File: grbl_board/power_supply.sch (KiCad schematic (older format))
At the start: 24 parts

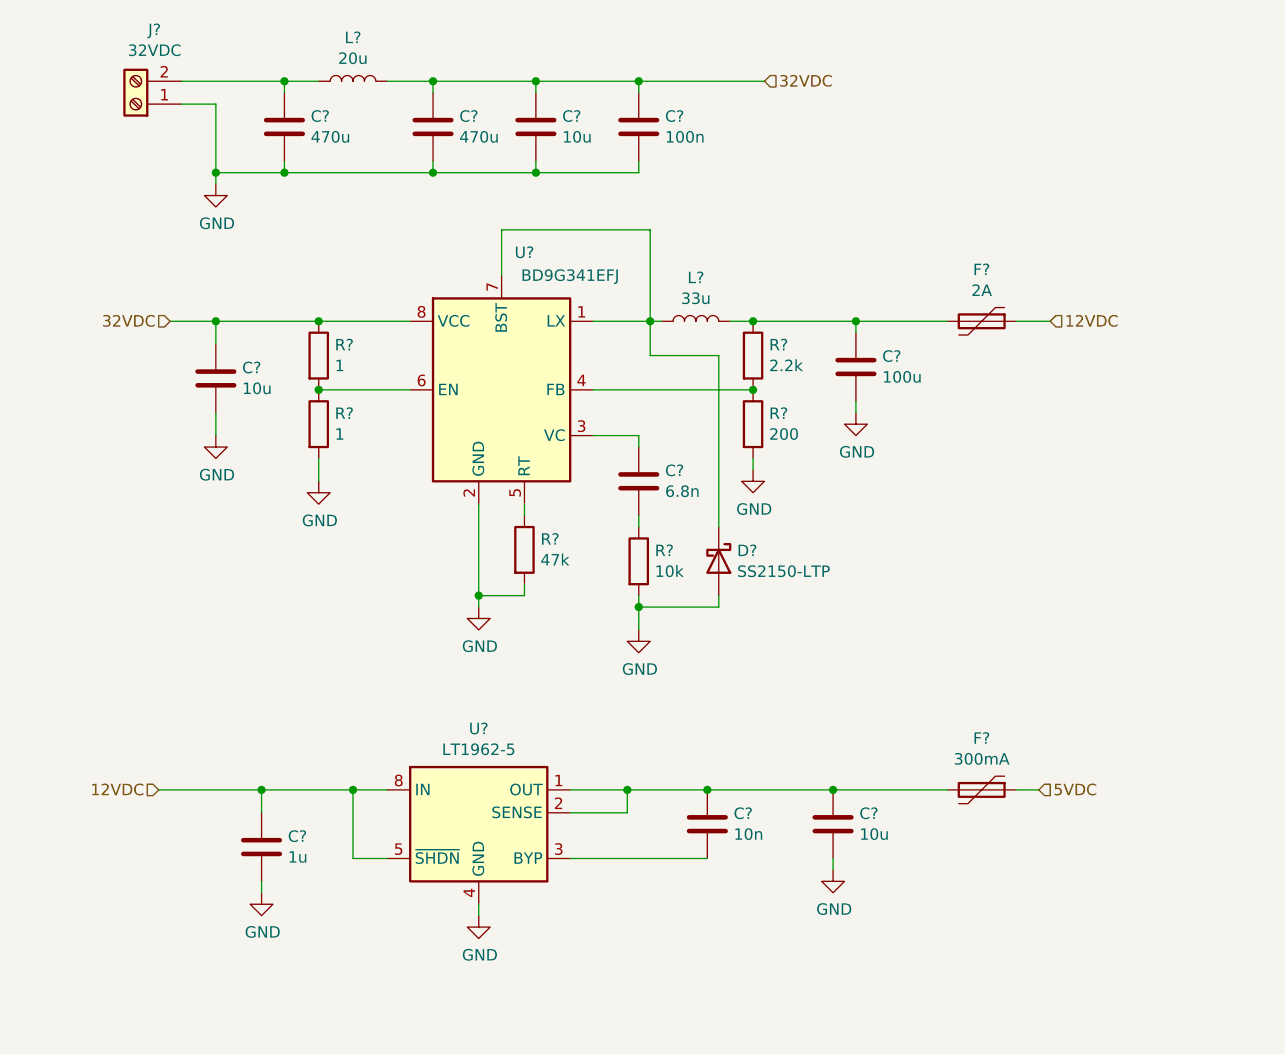
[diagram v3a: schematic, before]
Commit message: added some footprint associations
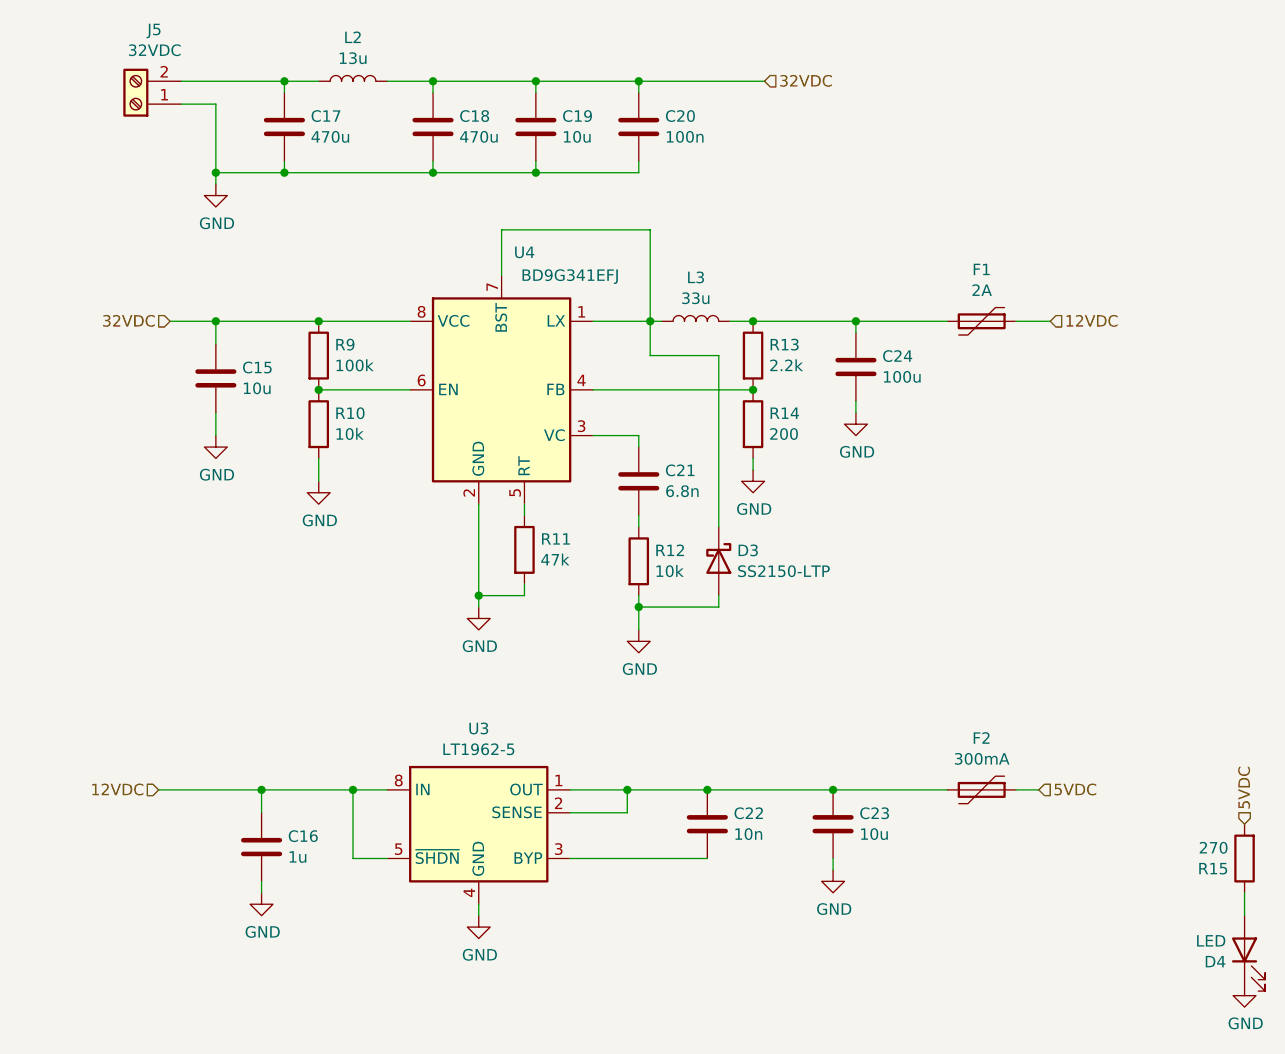
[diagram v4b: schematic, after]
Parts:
- added D4: LED, symbol Device:LED
- added R15: 270, Resistor_SMD:R_0805_2012Metric_Pad1.15x1.40mm_HandSolder, symbol Device:R
- C16: renamed from C?; footprint (none) -> Capacitor_SMD:C_1206_3216Metric_Pad1.33x1.80mm_HandSolder; Digikey Part No. (none) -> 1276-1204-1-ND
- C20: renamed from C?; footprint (none) -> Capacitor_SMD:C_0603_1608Metric_Pad1.05x0.95mm_HandSolder; Digikey Part No. (none) -> 1276-1941-1-ND
- C21: renamed from C?; footprint (none) -> Capacitor_SMD:C_0402_1005Metric_Pad0.74x0.62mm_HandSolder; Digikey Part No. (none) -> 1276-CL05B682KB5VPNCCT-ND
- C22: renamed from C?; footprint (none) -> Capacitor_SMD:C_1206_3216Metric_Pad1.33x1.80mm_HandSolder; Digikey Part No. (none) -> CL31F105ZBFNNNE
- J5: renamed from J?; footprint (none) -> Connector_Phoenix_MC:PhoenixContact_MC_1,5_2-G-3.81_1x02_P3.81mm_Horizontal; Digikey Part No. (none) -> ED2808-ND
- L2: renamed from L?; value 20u -> 13u; footprint (none) -> Inductor_SMD:L_Wuerth_HCI-1365; Digikey Part No. (none) -> 732-1140-1-ND
- L3: renamed from L?; footprint (none) -> Inductor_SMD:L_Vishay_IHLP-4040; Digikey Part No. (none) -> 541-2273-1-ND
- R10: renamed from R?; value 1 -> 10k; footprint (none) -> Resistor_SMD:R_0805_2012Metric_Pad1.15x1.40mm_HandSolder; Digikey Part No. (none) -> 311-10KARCT-ND
- R11: renamed from R?; footprint (none) -> Resistor_SMD:R_0805_2012Metric_Pad1.15x1.40mm_HandSolder; Digikey Part No. (none) -> 311-47KARCT-ND
- R12: renamed from R?; footprint (none) -> Resistor_SMD:R_0805_2012Metric_Pad1.15x1.40mm_HandSolder; Digikey Part No. (none) -> 311-10KARCT-ND
- R13: renamed from R?; footprint (none) -> Resistor_SMD:R_0603_1608Metric_Pad0.98x0.95mm_HandSolder; Digikey Part No. (none) -> 311-2.2KGRCT-ND
- R14: renamed from R?; footprint (none) -> Resistor_SMD:R_0603_1608Metric_Pad0.98x0.95mm_HandSolder; Digikey Part No. (none) -> 311-200GRCT-ND
- R9: renamed from R?; value 1 -> 100k; footprint (none) -> Resistor_SMD:R_0603_1608Metric_Pad0.98x0.95mm_HandSolder; Digikey Part No. (none) -> 311-100KGRCT-ND
- gave numbers to parts that had none: 11
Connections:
- net 5VDC: now also R15.2
- net GND: now also D4.1 (K)
- new net: D4.2 (A), R15.1

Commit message: complete footprint associations
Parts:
- removed C15, C19, C23: 10u, symbol Device:C
- removed C17, C18: 470u, symbol Device:C
- removed C24: 100u, symbol Device:C
- added C15, C19, C23: 10u, Capacitor_THT:CP_Radial_D8.0mm_P3.50mm, symbol Device:CP
- added C17, C18: 470u, Capacitor_THT:CP_Radial_D12.5mm_P5.00mm, symbol Device:CP
- added C24: 100u, Capacitor_THT:CP_Radial_D8.0mm_P3.50mm, symbol Device:CP
- D3: footprint (none) -> Diode_SMD:D_SMA_Handsoldering; Digikey Part No. (none) -> SS2150-LTPMSCT-ND
- D4: footprint (none) -> LED_SMD:LED_1206_3216Metric_Pad1.42x1.75mm_HandSolder; Digikey Part No. (none) -> 404-1046-1-ND
- F1: footprint (none) -> Fuse:Fuse_Bourns_MF-RHT200; Digikey Part No. (none) -> 118-MF-RHT200/32-0-ND
- F2: footprint (none) -> Fuse:Fuse_1812_4532Metric_Castellated; Digikey Part No. (none) -> 507-1758-1-ND
- U3: Digikey Part No. (none) -> LT1962EMS8-5#TRPBFCT-ND
- U4: Digikey Part No. (none) -> BD9G341AEFJ-E2CT-ND
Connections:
- net 32VDC: now also C15.1, C18.1, C19.1
- net GND: now also C15.2, C17.2, C18.2, C19.2, C23.2, C24.2
- net at J5.2 (Pin_2), L2.1: now also C17.1
- net at F1.2, L3.2, R13.1: now also C24.1
- net at C22.1, F2.2, U3.1 (OUT)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: now also C23.1
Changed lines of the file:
@@
 F 2 "Package_SO:HTSOP-8-1EP_3.9x4.9mm_P1.27mm_EP2.4x3.2mm_ThermalVias" H 5300 2650 50  0001 L CNN
 F 3 "https://media.digikey.com/pdf/Data%20Sheets/Rohm%20PDFs/BD9G341EFJ.pdf" H 5200 3100 50  0001 C CNN
+F 4 "BD9G341AEFJ-E2CT-ND" H 5200 3100 50  0001 C CNN "Digikey Part No."
 	1    5200 3100
 	1    0    0    -1
@@
 Wire Wire Line
 	3950 1850 3800 1850
-$Comp
-L Device:C C18
-U 1 1 617AA9A8
-P 4900 1950
-F 0 "C18" H 5015 1996 50  0000 L CNN
-F 1 "470u" H 5015 1905 50  0000 L CNN
-F 2 "" H 4938 1800 50  0001 C CNN
-F 3 "~" H 4900 1950 50  0001 C CNN
-	1    4900 1950
-	1    0    0    -1
-$EndComp
-$Comp
-L Device:C C19
-U 1 1 617AB129
-P 5350 1950
-F 0 "C19" H 5465 1996 50  0000 L CNN
-F 1 "10u" H 5465 1905 50  0000 L CNN
-F 2 "" H 5388 1800 50  0001 C CNN
-F 3 "~" H 5350 1950 50  0001 C CNN
-	1    5350 1950
-	1    0    0    -1
-$EndComp
 Wire Wire Line
 	5350 2150 5350 2100
@@
 Wire Wire Line
 	5800 1750 6350 1750
-$Comp
-L Device:C C17
-U 1 1 617B160B
-P 4250 1950
-F 0 "C17" H 4365 1996 50  0000 L CNN
-F 1 "470u" H 4365 1905 50  0000 L CNN
-F 2 "" H 4288 1800 50  0001 C CNN
-F 3 "~" H 4250 1950 50  0001 C CNN
-	1    4250 1950
-	1    0    0    -1
-$EndComp
 Wire Wire Line
 	3800 1750 4250 1750
@@
 Wire Wire Line
 	4400 3500 4400 3400
-$Comp
-L Device:C C15
-U 1 1 617B86C0
-P 3950 3050
-F 0 "C15" H 4065 3096 50  0000 L CNN
-F 1 "10u" H 4065 3005 50  0000 L CNN
-F 2 "" H 3988 2900 50  0001 C CNN
-F 3 "~" H 3950 3050 50  0001 C CNN
-	1    3950 3050
-	1    0    0    -1
-$EndComp
 Wire Wire Line
 	3950 2900 3950 2800
@@
 Wire Wire Line
 	6300 2800 6750 2800
-$Comp
-L Device:C C24
-U 1 1 617C1EFE
-P 6750 3000
-F 0 "C24" H 6865 3046 50  0000 L CNN
-F 1 "100u" H 6865 2955 50  0000 L CNN
-F 2 "" H 6788 2850 50  0001 C CNN
-F 3 "~" H 6750 3000 50  0001 C CNN
-	1    6750 3000
-	1    0    0    -1
-$EndComp
 Wire Wire Line
 	6750 2850 6750 2800
@@
 F 0 "D3" V 6104 3930 50  0000 L CNN
 F 1 "SS2150-LTP" V 6195 3930 50  0000 L CNN
-F 2 "" H 6150 3850 50  0001 C CNN
-F 3 "~" H 6150 3850 50  0001 C CNN
+F 2 "Diode_SMD:D_SMA_Handsoldering" H 6150 3850 50  0001 C CNN
+F 3 "https://www.mccsemi.com/pdf/Products/SS22-L-SS220-L(DO-214AC).pdf" H 6150 3850 50  0001 C CNN
+F 4 "SS2150-LTPMSCT-ND" H 6150 3850 50  0001 C CNN "Digikey Part No."
 	1    6150 3850
 	0    1    1    0
@@
 F 2 "Package_SO:MSOP-8_3x3mm_P0.65mm" H 5100 4700 50  0001 C CNN
 F 3 "https://www.analog.com/media/en/technical-documentation/data-sheets/1962fb.pdf" H 5100 4500 50  0001 C CNN
+F 4 "LT1962EMS8-5#TRPBFCT-ND" H 5100 5050 50  0001 C CNN "Digikey Part No."
 	1    5100 5050
 	1    0    0    -1
@@
 	1    0    0    -1
 $EndComp
-$Comp
-L Device:C C23
-U 1 1 617E5C2A
-P 6650 5000
-F 0 "C23" H 6765 5046 50  0000 L CNN
-F 1 "10u" H 6765 4955 50  0000 L CNN
-F 2 "" H 6688 4850 50  0001 C CNN
-F 3 "~" H 6650 5000 50  0001 C CNN
-	1    6650 5000
-	1    0    0    -1
-$EndComp
 Wire Wire Line
 	6100 5150 5500 5150
-Wire Wire Line
-	6650 4850 6100 4850
-Connection ~ 6100 4850
 Wire Wire Line
 	6100 4850 5750 4850
@@
 F 0 "F1" V 7075 2800 50  0000 C CNN
 F 1 "2A" V 7166 2800 50  0000 C CNN
-F 2 "" H 7350 2600 50  0001 L CNN
-F 3 "~" H 7300 2800 50  0001 C CNN
+F 2 "Fuse:Fuse_Bourns_MF-RHT200" H 7350 2600 50  0001 L CNN
+F 3 "https://www.bourns.com/docs/product-datasheets/mfrht.pdf" H 7300 2800 50  0001 C CNN
+F 4 "118-MF-RHT200/32-0-ND" H 7300 2800 50  0001 C CNN "Digikey Part No."
 	1    7300 2800
 	0    1    1    0
@@
 F 0 "F2" V 7075 4850 50  0000 C CNN
 F 1 "300mA" V 7166 4850 50  0000 C CNN
-F 2 "" H 7350 4650 50  0001 L CNN
-F 3 "~" H 7300 4850 50  0001 C CNN
+F 2 "Fuse:Fuse_1812_4532Metric_Castellated" H 7350 4650 50  0001 L CNN
+F 3 "https://www.belfuse.com/resources/datasheets/circuitprotection/ds-cp-0zcg-series.pdf" H 7300 4850 50  0001 C CNN
+F 4 "507-1758-1-ND" H 7300 4850 50  0001 C CNN "Digikey Part No."
 	1    7300 4850
 	0    1    1    0
 $EndComp
-Wire Wire Line
-	7150 4850 6650 4850
-Connection ~ 6650 4850
 Wire Wire Line
 	7550 4850 7450 4850
@@
 F 0 "D4" V 8397 5630 50  0000 L CNN
 F 1 "LED" V 8488 5630 50  0000 L CNN
-F 2 "" H 8450 5550 50  0001 C CNN
-F 3 "~" H 8450 5550 50  0001 C CNN
+F 2 "LED_SMD:LED_1206_3216Metric_Pad1.42x1.75mm_HandSolder" H 8450 5550 50  0001 C CNN
+F 3 "https://media.digikey.com/pdf/Data%20Sheets/Stanley%20Electric%20PDFs/1101W_Series.pdf" H 8450 5550 50  0001 C CNN
+F 4 "404-1046-1-ND" H 8450 5550 50  0001 C CNN "Digikey Part No."
 	1    8450 5550
 	0    -1   -1   0
@@
 Text HLabel 8450 5000 1    50   Input ~ 0
 5VDC
+$Comp
+L Device:CP C17
+U 1 1 61B06178
+P 4250 1950
+F 0 "C17" H 4368 1996 50  0000 L CNN
+F 1 "470u" H 4368 1905 50  0000 L CNN
+F 2 "Capacitor_THT:CP_Radial_D12.5mm_P5.00mm" H 4288 1800 50  0001 C CNN
+F 3 "https://www.tdk-electronics.tdk.com/inf/20/30/db/aec/B41896.pdf?ref_disty=digikey" H 4250 1950 50  0001 C CNN
+F 4 "B41896C7477M000-ND" H 4250 1950 50  0001 C CNN "Digikey Part No."
+	1    4250 1950
+	1    0    0    -1
+$EndComp
+$Comp
+L Device:CP C18
+U 1 1 61B09554
+P 4900 1950
+F 0 "C18" H 5018 1996 50  0000 L CNN
+F 1 "470u" H 5018 1905 50  0000 L CNN
+F 2 "Capacitor_THT:CP_Radial_D12.5mm_P5.00mm" H 4938 1800 50  0001 C CNN
+F 3 "https://www.tdk-electronics.tdk.com/inf/20/30/db/aec/B41896.pdf?ref_disty=digikey" H 4900 1950 50  0001 C CNN
+F 4 "B41896C7477M000-ND" H 4900 1950 50  0001 C CNN "Digikey Part No."
+	1    4900 1950
+	1    0    0    -1
+$EndComp
+$Comp
+L Device:CP C15
+U 1 1 61B0C9E2
+P 3950 3050
+F 0 "C15" H 4068 3096 50  0000 L CNN
+F 1 "10u" H 4068 3005 50  0000 L CNN
+F 2 "Capacitor_THT:CP_Radial_D8.0mm_P3.50mm" H 3988 2900 50  0001 C CNN
+F 3 "https://www.tdk-electronics.tdk.com/inf/20/30/db/aec/B41866.pdf?ref_disty=digikey" H 3950 3050 50  0001 C CNN
+F 4 "495-75596-ND" H 3950 3050 50  0001 C CNN "Digikey Part No."
+	1    3950 3050
+	1    0    0    -1
+$EndComp
+$Comp
+L Device:CP C24
+U 1 1 61B10617
+P 6750 3000
+F 0 "C24" H 6868 3046 50  0000 L CNN
+F 1 "100u" H 6868 2955 50  0000 L CNN
+F 2 "Capacitor_THT:CP_Radial_D8.0mm_P3.50mm" H 6788 2850 50  0001 C CNN
+F 3 "https://www.tdk-electronics.tdk.com/inf/20/30/db/aec_2013/B41821_B43821.pdf" H 6750 3000 50  0001 C CNN
+F 4 "495-5986-ND" H 6750 3000 50  0001 C CNN "Digikey Part No."
+	1    6750 3000
+	1    0    0    -1
+$EndComp
+$Comp
+L Device:CP C23
+U 1 1 61B13999
+P 6650 5000
+F 0 "C23" H 6768 5046 50  0000 L CNN
+F 1 "10u" H 6768 4955 50  0000 L CNN
+F 2 "Capacitor_THT:CP_Radial_D8.0mm_P3.50mm" H 6688 4850 50  0001 C CNN
+F 3 "https://www.tdk-electronics.tdk.com/inf/20/30/db/aec/B41866.pdf?ref_disty=digikey" H 6650 5000 50  0001 C CNN
+F 4 "495-75596-ND" H 6650 5000 50  0001 C CNN "Digikey Part No."
+	1    6650 5000
+	1    0    0    -1
+$EndComp
+Wire Wire Line
+	7150 4850 6650 4850
+Wire Wire Line
+	6100 4850 6650 4850
+Connection ~ 6100 4850
+Connection ~ 6650 4850
+$Comp
+L Device:CP C19
+U 1 1 61B8AB5A
+P 5350 1950
+F 0 "C19" H 5468 1996 50  0000 L CNN
+F 1 "10u" H 5468 1905 50  0000 L CNN
+F 2 "Capacitor_THT:CP_Radial_D8.0mm_P3.50mm" H 5388 1800 50  0001 C CNN
+F 3 "https://www.tdk-electronics.tdk.com/inf/20/30/db/aec/B41866.pdf?ref_disty=digikey" H 5350 1950 50  0001 C CNN
+F 4 "495-75596-ND" H 5350 1950 50  0001 C CNN "Digikey Part No."
+	1    5350 1950
+	1    0    0    -1
+$EndComp
 $EndSCHEMATC

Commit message: routing done
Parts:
- removed J5: 32VDC, Connector_Phoenix_MC:PhoenixContact_MC_1,5_2-G-3.81_1x02_P3.81mm_Horizontal, symbol Connector:Screw_Terminal_01x02
- added J5: Screw_Terminal_01x04, Connector_Phoenix_MC:PhoenixContact_MC_1,5_4-G-3.81_1x04_P3.81mm_Horizontal, symbol Connector:Screw_Terminal_01x04
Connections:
- net GND: now also J5.1 (Pin_1), J5.2 (Pin_2)
- net at C17.1, L2.1: now also J5.3 (Pin_3), J5.4 (Pin_4)
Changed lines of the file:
@@
-$EndComp
-$Comp
-L Connector:Screw_Terminal_01x02 J5
-U 1 1 617A7AB6
-P 3600 1850
-F 0 "J5" H 3518 1525 50  0000 C CNN
-F 1 "32VDC" H 3518 1616 50  0000 C CNN
-F 2 "Connector_Phoenix_MC:PhoenixContact_MC_1,5_2-G-3.81_1x02_P3.81mm_Horizontal" H 3600 1850 50  0001 C CNN
-F 3 "https://www.on-shore.com/wp-content/uploads/OSTOQXX3251.pdf" H 3600 1850 50  0001 C CNN
-F 4 "ED2808-ND" H 3600 1850 50  0001 C CNN "Digikey Part No."
-	1    3600 1850
-	-1   0    0    1
 $EndComp
 $Comp
@@
 $EndComp
 Wire Wire Line
-	3950 1850 3800 1850
-Wire Wire Line
 	5350 2150 5350 2100
 Wire Wire Line
@@
 Text HLabel 6350 1750 2    50   Input ~ 0
 32VDC
-Wire Wire Line
-	3950 1850 3950 2150
 $Comp
 L Device:L L2
@@
 Wire Wire Line
 	3950 2150 4250 2150
-Connection ~ 3950 2150
 Wire Wire Line
 	3950 2150 3950 2200
@@
 	1    0    0    -1
 $EndComp
+$Comp
+L Connector:Screw_Terminal_01x04 J5
+U 1 1 61EF7F56
+P 3500 1950
+F 0 "J5" H 3418 1525 50  0000 C CNN
+F 1 "Screw_Terminal_01x04" H 3418 1616 50  0000 C CNN
+F 2 "Connector_Phoenix_MC:PhoenixContact_MC_1,5_4-G-3.81_1x04_P3.81mm_Horizontal" H 3500 1950 50  0001 C CNN
+F 3 "https://www.on-shore.com/wp-content/uploads/OSTOQXX3251.pdf" H 3500 1950 50  0001 C CNN
+F 4 "ED2810-ND" H 3500 1950 50  0001 C CNN "Digikey Part No."
+	1    3500 1950
+	-1   0    0    1
+$EndComp
+Wire Wire Line
+	3700 1950 3950 1950
+Wire Wire Line
+	3950 1950 3950 2050
+Connection ~ 3950 2150
+Wire Wire Line
+	3950 2050 3700 2050
+Connection ~ 3950 2050
+Wire Wire Line
+	3950 2050 3950 2150
+Wire Wire Line
+	3700 1850 3800 1850
+Wire Wire Line
+	3800 1850 3800 1750
+Wire Wire Line
+	3800 1750 3700 1750
+Connection ~ 3800 1750
 $EndSCHEMATC

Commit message: updated README
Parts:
- C22: footprint Capacitor_SMD:C_1206_3216Metric_Pad1.33x1.80mm_HandSolder -> Capacitor_SMD:C_0603_1608Metric_Pad1.08x0.95mm_HandSolder; Digikey Part No. CL31F105ZBFNNNE -> 1276-1009-1-ND
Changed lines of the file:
@@
 F 0 "C22" H 6215 5046 50  0000 L CNN
 F 1 "10n" H 6215 4955 50  0000 L CNN
-F 2 "Capacitor_SMD:C_1206_3216Metric_Pad1.33x1.80mm_HandSolder" H 6138 4850 50  0001 C CNN
+F 2 "Capacitor_SMD:C_0603_1608Metric_Pad1.08x0.95mm_HandSolder" H 6138 4850 50  0001 C CNN
 F 3 "http://www.samsungsem.com/kr/support/product-search/mlcc/CL31F105ZBFNNNE.jsp" H 6100 5000 50  0001 C CNN
-F 4 "CL31F105ZBFNNNE" H 6100 5000 50  0001 C CNN "Digikey Part No."
+F 4 "1276-1009-1-ND" H 6100 5000 50  0001 C CNN "Digikey Part No."
 	1    6100 5000
 	1    0    0    -1

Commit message: added some descriptions in the schematic and added gerber file
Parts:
- C17, C18: Digikey Part No. B41896C7477M000-ND -> 495-76603-ND
- C24: Digikey Part No. 495-5986-ND -> 399-6119-ND
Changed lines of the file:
@@
 F 1 "470u" H 4368 1905 50  0000 L CNN
 F 2 "Capacitor_THT:CP_Radial_D12.5mm_P5.00mm" H 4288 1800 50  0001 C CNN
-F 3 "https://www.tdk-electronics.tdk.com/inf/20/30/db/aec/B41896.pdf?ref_disty=digikey" H 4250 1950 50  0001 C CNN
-F 4 "B41896C7477M000-ND" H 4250 1950 50  0001 C CNN "Digikey Part No."
+F 3 "https://www.tdk-electronics.tdk.com/inf/20/30/db/aec/B41895.pdf" H 4250 1950 50  0001 C CNN
+F 4 "495-76603-ND" H 4250 1950 50  0001 C CNN "Digikey Part No."
 	1    4250 1950
 	1    0    0    -1
@@
 F 1 "470u" H 5018 1905 50  0000 L CNN
 F 2 "Capacitor_THT:CP_Radial_D12.5mm_P5.00mm" H 4938 1800 50  0001 C CNN
-F 3 "https://www.tdk-electronics.tdk.com/inf/20/30/db/aec/B41896.pdf?ref_disty=digikey" H 4900 1950 50  0001 C CNN
-F 4 "B41896C7477M000-ND" H 4900 1950 50  0001 C CNN "Digikey Part No."
+F 3 "https://www.tdk-electronics.tdk.com/inf/20/30/db/aec/B41895.pdf" H 4900 1950 50  0001 C CNN
+F 4 "495-76603-ND" H 4900 1950 50  0001 C CNN "Digikey Part No."
 	1    4900 1950
 	1    0    0    -1
@@
 F 1 "100u" H 6868 2955 50  0000 L CNN
 F 2 "Capacitor_THT:CP_Radial_D8.0mm_P3.50mm" H 6788 2850 50  0001 C CNN
-F 3 "https://www.tdk-electronics.tdk.com/inf/20/30/db/aec_2013/B41821_B43821.pdf" H 6750 3000 50  0001 C CNN
-F 4 "495-5986-ND" H 6750 3000 50  0001 C CNN "Digikey Part No."
+F 3 "https://api.kemet.com/component-edge/download/specsheet/ESY107M050AG3AA.pdf" H 6750 3000 50  0001 C CNN
+F 4 "399-6119-ND" H 6750 3000 50  0001 C CNN "Digikey Part No."
 	1    6750 3000
 	1    0    0    -1
